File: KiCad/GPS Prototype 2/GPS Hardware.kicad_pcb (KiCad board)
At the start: 4 copper layers, 80 x 80 mm, 73 parts, among them J1 USB_C_Receptacle_USB2.0, J2 Conn_01x06_Male, J3 Conn_Coaxial, J4 SIM8065-6-1-14-01-A_REVA1, J5 B2B-XH-A(LF)(SN), Q1 BC847, Q2 BC847, Q3 BSS84, U10 ublox_SAM-M8Q, U3 BQ24295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

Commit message: updated
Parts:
- added U1: ESD122DMX, GPS Hardware:IC_ESD122DMXR, F.Cu at (177.2, 75.8)
- C10, C11, C12, C13, C16, C17, C18, C19, C20, C21, C22, C23: footprint Capacitor_SMD:C_0402_1005Metric_Pad0.74x0.62mm_HandSolder -> Capacitor_SMD:C_0805_2012Metric
- C14, C15: footprint Capacitor_SMD:C_0603_1608Metric_Pad1.08x0.95mm_HandSolder -> Capacitor_SMD:C_0805_2012Metric
- J2: value Conn_01x06_Male -> TSM-103-01-L-DV-P-TR; footprint Connector_PinHeader_1.00mm:PinHeader_2x03_P1.00mm_Vertical_SMD -> GPS Hardware:SAMTEC_TSM-103-01-L-DV-P-TR
- R12, R13, R14, R15, R16, R20: footprint Resistor_SMD:R_0402_1005Metric_Pad0.72x0.64mm_HandSolder -> Resistor_SMD:R_0805_2012Metric
- R17, R18, R19: footprint Resistor_SMD:R_0603_1608Metric_Pad0.98x0.95mm_HandSolder -> Resistor_SMD:R_0805_2012Metric
- moved C9 23.9 mm to (143.1, 91.5)
- moved U4 23.4 mm to (139.2, 91.5)
- moved R15 22.6 mm to (162.9, 110.3)
- moved C13 21.6 mm to (167.9, 102.3)
- moved C12 21.4 mm to (167.9, 98.0)
- moved R5 20.1 mm to (162.3, 88.5), turned to 90 degrees
- moved R3 20.1 mm to (159.3, 110.2)
- moved U5 19.1 mm to (159.5, 99.3)
- moved R14 18.2 mm to (151.4, 88.9)
- moved C14 18.0 mm to (164.9, 92.8)
- moved R4 17.6 mm to (155.7, 110.2)
- moved C10 17.0 mm to (151.4, 100.3)
- moved C11 16.9 mm to (151.3, 95.8), turned to 90 degrees
- moved R12 16.1 mm to (157.2, 89.2)
- moved R13 16.1 mm to (156.2, 89.3)
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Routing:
- net IO: track 38.5 -> 1.41 mm, vias 0 -> 1
- net CLK: track 37.7 -> 1.43 mm, vias 0 -> 1
- net Net-(R9-Pad1): track 35.0 -> 0.58 mm
- net VSIM: track 28.6 -> 1.39 mm, vias 0 -> 1
- net RST: track 27.7 -> 1.37 mm, vias 0 -> 1
- net Net-(R10-Pad2): track 6.97 -> 0.00 mm
- net Net-(C4-Pad1): track 6.26 -> 0.00 mm
- net Net-(R6-Pad1): track 5.64 -> 0.00 mm
- net Net-(R7-Pad2): track 4.08 -> 0.00 mm
- net Net-(C3-Pad1): track 3.99 -> 0.00 mm
- net Net-(C2-Pad1): track 2.78 -> 0.00 mm
- net GND: vias 0 -> 4

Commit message: Update to PC
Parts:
- removed U1: ESD122DMX, GPS Hardware:IC_ESD122DMXR
- moved C15 18.6 mm to (157.0, 80.0)
- moved Y1 18.0 mm to (161.2, 83.5)
- moved U4 12.2 mm to (127.6, 95.6)
- moved C9 12.2 mm to (131.5, 95.6)
- moved C8 12.2 mm to (123.5, 95.5)
- moved R5 10.8 mm to (151.6, 89.6)
- moved C13 10.4 mm to (157.6, 101.1)
- moved C12 10.4 mm to (157.6, 96.8)
- moved J2 10.3 mm to (148.9, 75.4), turned to 180 degrees
- moved R16 10.2 mm to (142.2, 107.5)
- moved R3 10.2 mm to (149.5, 107.4)
- moved R4 10.2 mm to (145.8, 107.4)
- moved R15 10.2 mm to (153.1, 107.4)
- moved C10 9.96 mm to (141.5, 99.0)
- moved C11 9.96 mm to (141.5, 94.5)
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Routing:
- net Net-(C4-Pad1): track 0.00 -> 9.57 mm
- net Net-(C3-Pad1): track 0.00 -> 2.74 mm
- net Net-(C2-Pad1): track 0.00 -> 2.48 mm
- net CLK: track 1.43 -> 0.00 mm
- net IO: track 1.41 -> 0.00 mm
- net RST: track 1.37 -> 0.00 mm
- net VSIM: track 1.39 -> 0.03 mm

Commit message: Update to laptop
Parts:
- moved D2 10.8 mm to (131.8, 127.9)
- moved R19 7.09 mm to (136.7, 127.9), turned to 180 degrees
- moved R18 6.72 mm to (126.7, 120.1), turned to 90 degrees
- moved Q1 4.99 mm to (129.9, 122.1)
- moved C5 4.37 mm to (106.1, 84.1), turned to 180 degrees
- moved J2 4.10 mm to (148.0, 71.4)
- moved R13 4.10 mm to (148.1, 80.3)
- moved R14 4.10 mm to (143.7, 80.3)
- moved R12 4.10 mm to (152.4, 80.3)
- moved C14 3.87 mm to (158.4, 93.0)
- moved Y1 3.87 mm to (157.5, 84.7)
- moved C15 3.78 mm to (158.1, 76.4), turned to 0 degrees
- moved R11 3.38 mm to (104.9, 80.9)
- moved R6 3.38 mm to (104.9, 70.9)
- moved R7 3.38 mm to (104.9, 74.5)
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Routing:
- added copper zone on F.Cu, net Net-(C5-Pad1)

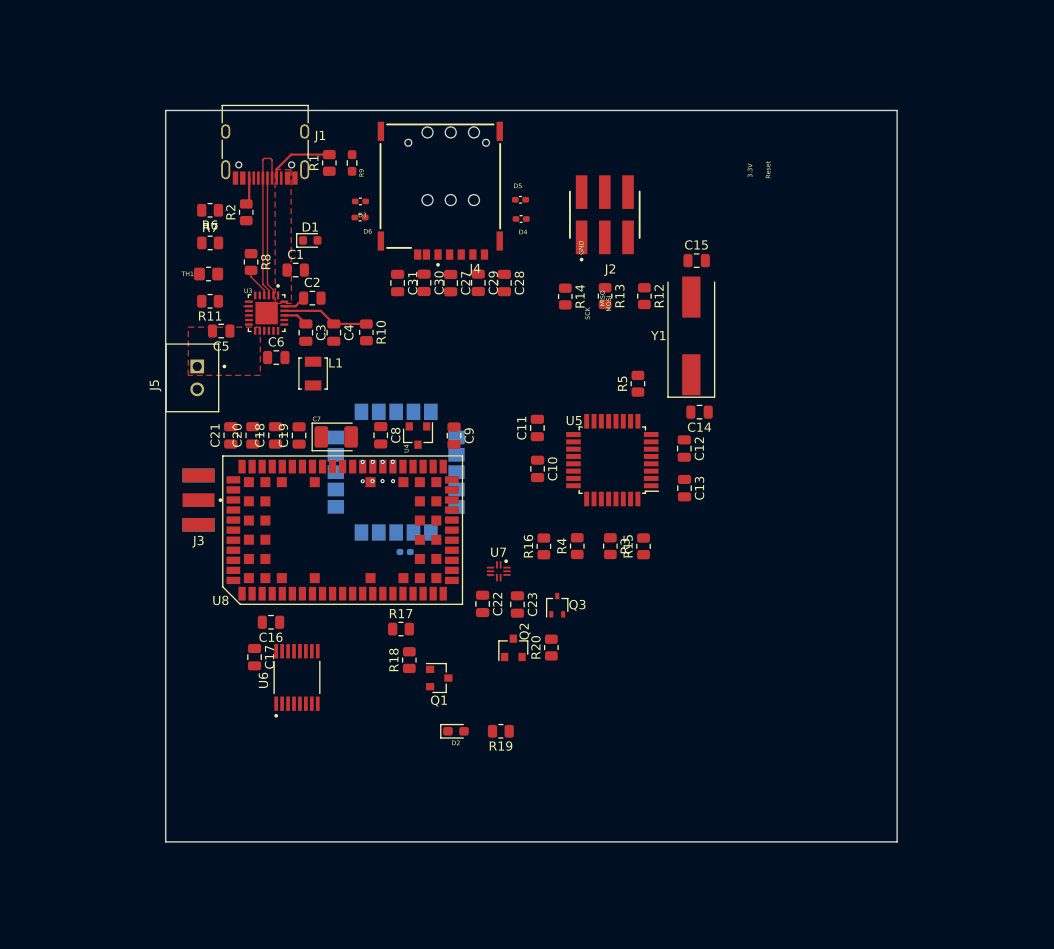
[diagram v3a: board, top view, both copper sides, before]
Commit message: Connected all the PCB connections and 20h distance
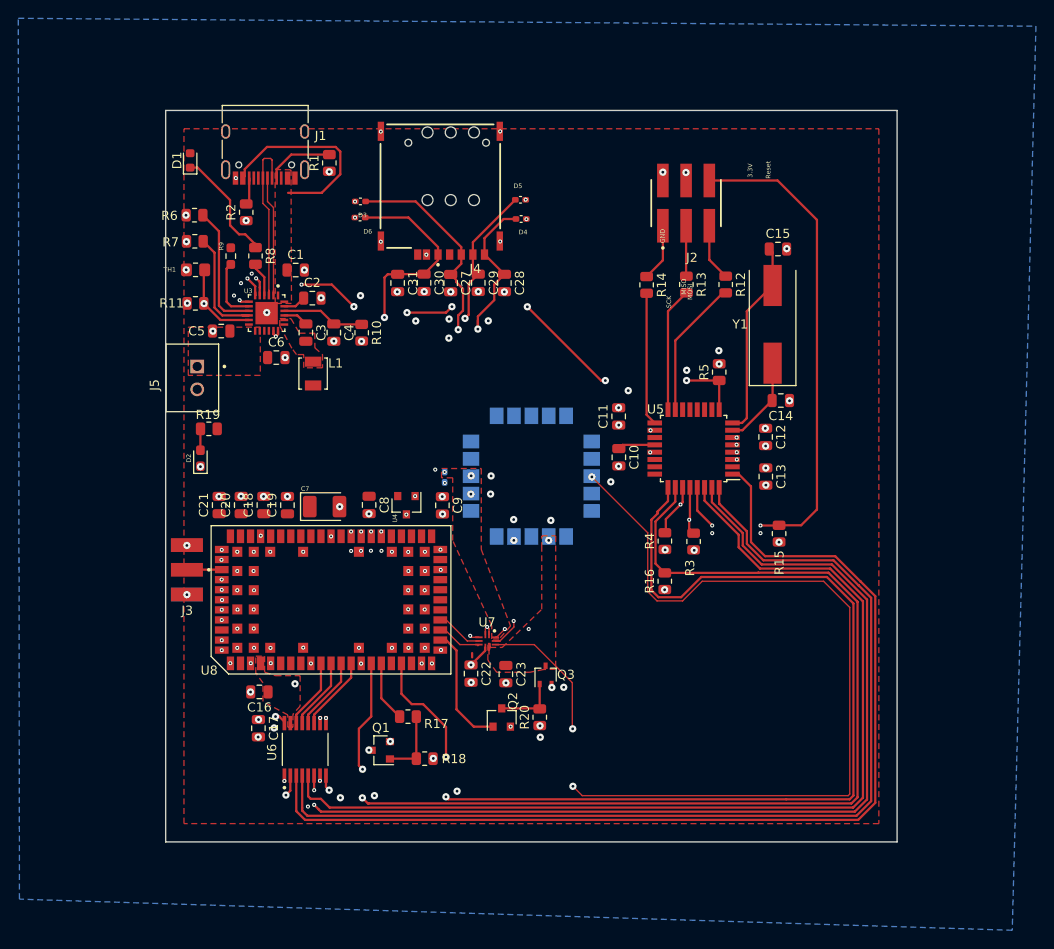
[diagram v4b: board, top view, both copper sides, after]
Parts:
- moved R19 46.0 mm to (104.7, 94.8)
- moved D2 40.9 mm to (103.8, 98.0), turned to 90 degrees
- moved R9 16.7 mm to (107.1, 75.9), turned to 90 degrees
- moved D1 15.8 mm to (102.7, 65.5), turned to 90 degrees
- moved R15 14.9 mm to (167.1, 106.3)
- moved U10 14.8 mm to (140.0, 100.0)
- moved R16 13.8 mm to (154.6, 111.5)
- moved R18 10.9 mm to (128.3, 130.9), turned to 0 degrees
- moved Q1 10.2 mm to (123.5, 130.0), turned to 180 degrees
- moved R17 9.61 mm to (126.5, 126.3)
- moved R4 9.60 mm to (154.6, 107.1)
- moved C25 9.26 mm to (130.5, 100.1), turned to 270 degrees
- moved R3 9.12 mm to (157.7, 107.1)
- moved C12 8.98 mm to (165.6, 95.7)
- moved C14 8.98 mm to (167.3, 91.7)
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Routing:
- net SDA_Power: track 0.03 -> 148.8 mm, vias 0 -> 2
- net SCL_Power: track 0.26 -> 146.9 mm, vias 0 -> 2
- net PWR_Cellular: track 0.00 -> 124.6 mm, vias 0 -> 2
- net RESET_Cellular: track 0.00 -> 120.4 mm, vias 0 -> 2
- net CTS: track 0.00 -> 115.7 mm
- net RTS: track 0.00 -> 113.1 mm
- net TX_GPS: track 0.00 -> 112.4 mm, vias 0 -> 3
- net TX: track 0.00 -> 110.2 mm, vias 0 -> 2
- net RX: track 0.00 -> 109.5 mm
- net INT_Power: track 0.00 -> 62.8 mm, vias 0 -> 8
- net RESET: track 0.00 -> 62.3 mm, vias 0 -> 2
- net RST: track 0.00 -> 49.3 mm, vias 1 -> 2
- net Net-(D2-Pad1): track 0.00 -> 47.7 mm, vias 0 -> 2
- net VSIM: track 0.03 -> 46.7 mm, vias 1 -> 2
- net CLK: track 0.00 -> 43.8 mm, vias 1 -> 2
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- added copper zone on F.Cu, net +1V8
- added copper zone on In2.Cu, net +3V3
- added copper zone on B.Cu, net GND
- added copper zone on In1.Cu, net GND
- added copper zone on F.Cu, net Net-(C3-Pad2)
- added copper zone on F.Cu, net SYS
- added copper zone on F.Cu, net VCC_GPS
